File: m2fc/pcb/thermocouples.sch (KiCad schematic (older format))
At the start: 69 parts, among them IC301 AD8495, IC302 AD8656, IC303 AD8495, IC304 AD8656, IC305 AD8495, IC306 AD8656, P301 CONN_2, P302 CONN_2, P303 CONN_2

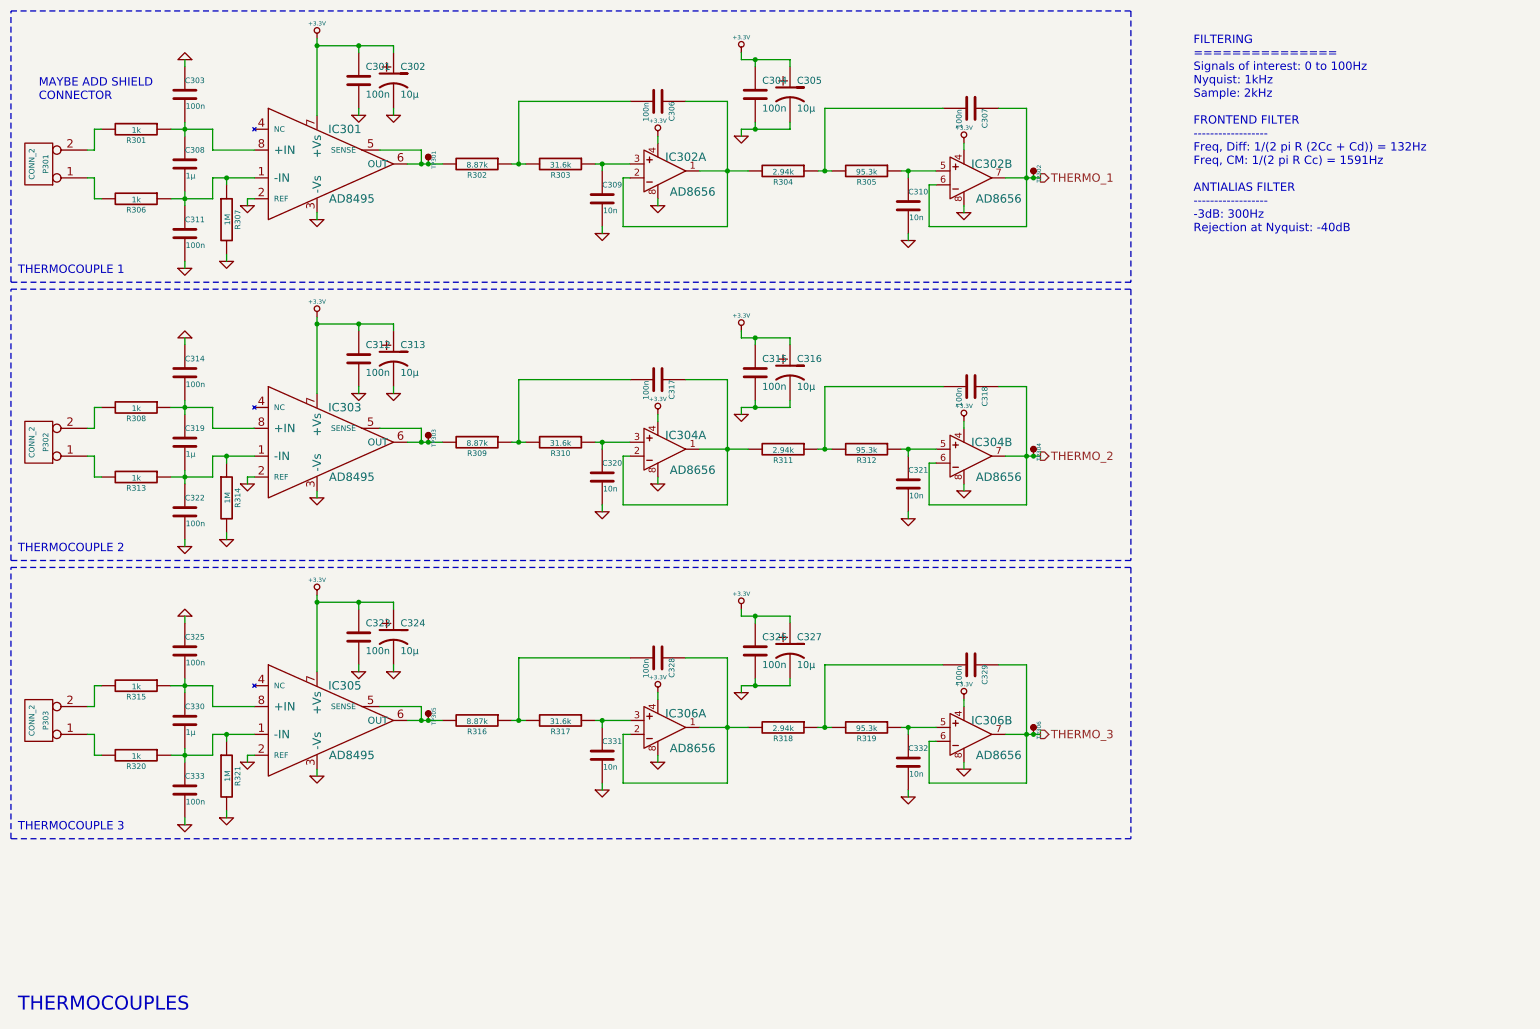
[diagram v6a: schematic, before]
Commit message: sd pullups, shielded sgs
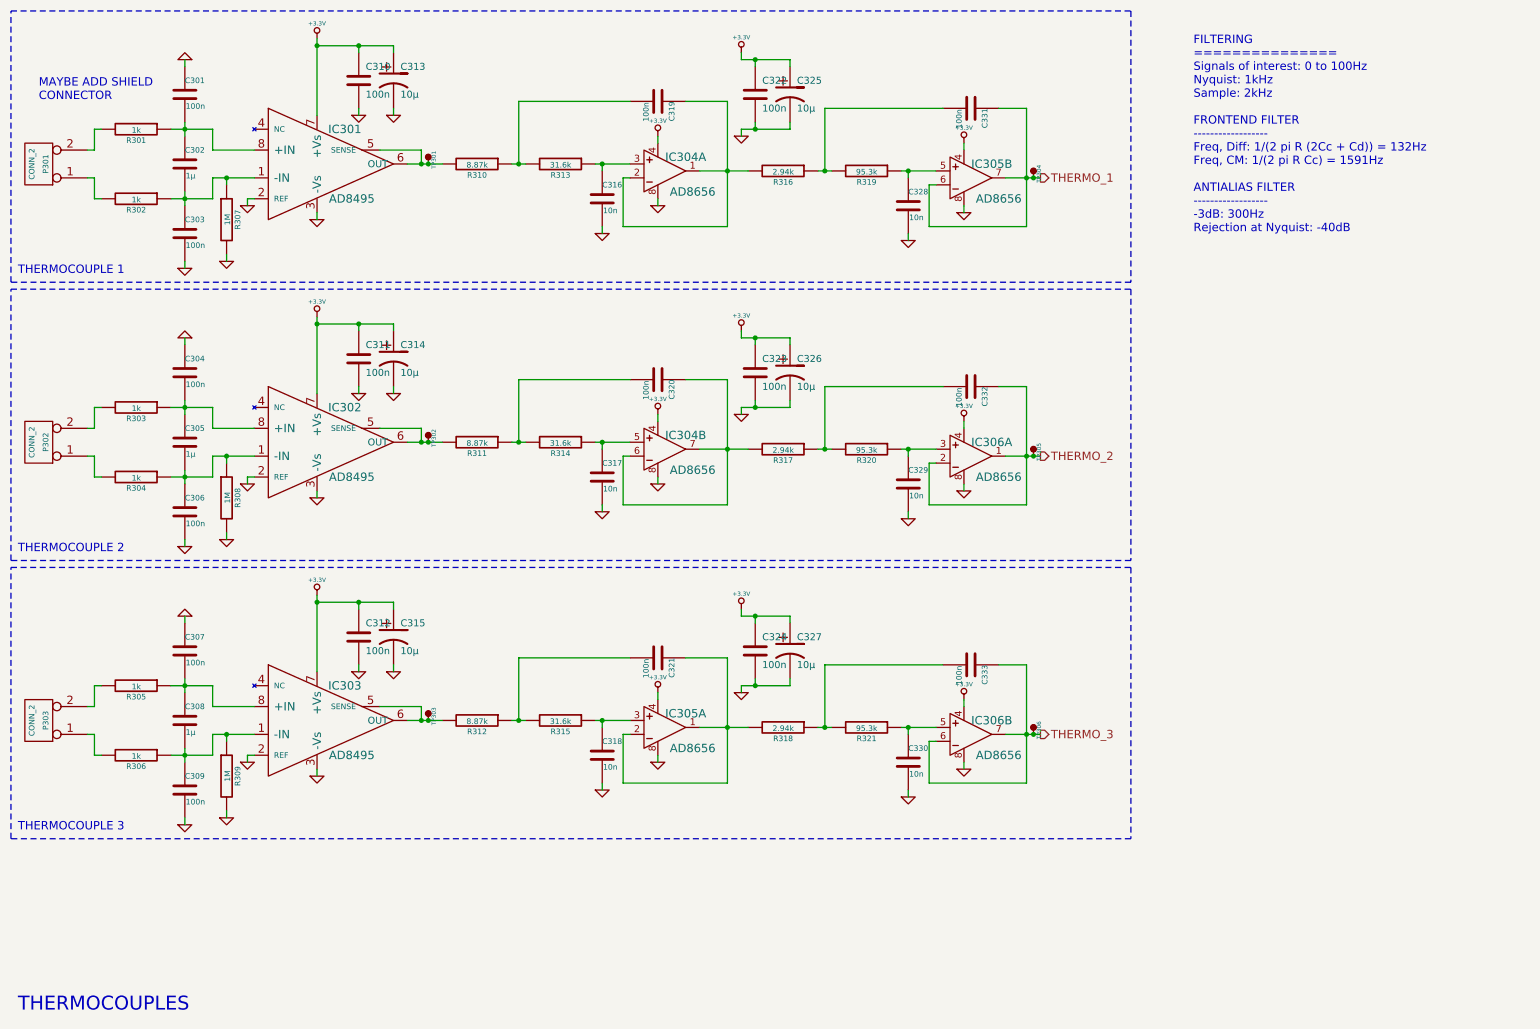
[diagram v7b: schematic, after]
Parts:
- C301: renamed from C303; footprint 1206 -> m2fc:C1206
- C302: renamed from C308; footprint 1206 -> m2fc:C1206
- C303: renamed from C311; footprint 1206 -> m2fc:C1206
- C304: renamed from C314; footprint 1206 -> m2fc:C1206
- C305: renamed from C319; footprint 1206 -> m2fc:C1206
- C306: renamed from C322; footprint 1206 -> m2fc:C1206
- C307: renamed from C325; footprint 1206 -> m2fc:C1206
- C308: renamed from C330; footprint 1206 -> m2fc:C1206
- C309: renamed from C333; footprint 1206 -> m2fc:C1206
- C310: renamed from C301; footprint 0603 -> m2fc:C0603
- C311: renamed from C312; footprint 0603 -> m2fc:C0603
- C312: renamed from C323; footprint 0603 -> m2fc:C0603
- C316: renamed from C309; footprint 0603 -> m2fc:C0603
- C317: renamed from C320; footprint 0603 -> m2fc:C0603
- C318: renamed from C331; footprint 0603 -> m2fc:C0603
- C319: renamed from C306; footprint 1206 -> m2fc:C1206
- C320: renamed from C317; footprint 1206 -> m2fc:C1206
- C321: renamed from C328; footprint 1206 -> m2fc:C1206
- C322: renamed from C304; footprint 0603 -> m2fc:C0603
- C323: renamed from C315; footprint 0603 -> m2fc:C0603
- C324: renamed from C326; footprint 0603 -> m2fc:C0603
- C328: renamed from C310; footprint 0603 -> m2fc:C0603
- C329: renamed from C321; footprint 0603 -> m2fc:C0603
- C330: renamed from C332; footprint 0603 -> m2fc:C0603
- C331: renamed from C307; footprint 1206 -> m2fc:C1206
- C332: renamed from C318; footprint 1206 -> m2fc:C1206
- C333: renamed from C329; footprint 1206 -> m2fc:C1206
- IC301: footprint 8MSOP -> m2fc:MSOP8
- IC302: renamed from IC303; footprint 8MSOP -> m2fc:MSOP8
- IC303: renamed from IC305; footprint 8MSOP -> m2fc:MSOP8
- IC304, IC305: renamed from IC302; footprint SOIC8 -> m2fc:SOIC8
- IC304, IC306: footprint SOIC8 -> m2fc:SOIC8
- IC305: renamed from IC306; footprint SOIC8 -> m2fc:SOIC8
- IC306: renamed from IC304; footprint SOIC8 -> m2fc:SOIC8
- P301, P302: footprint (none) -> m2fc:S02B-PASK-2
- P303: footprint (none) -> m2fc:S04B-PASK-2
- R301, R307, R318: footprint 0603 -> m2fc:R0603
- R302: renamed from R306; footprint 0603 -> m2fc:R0603
- R303: renamed from R308; footprint 0603 -> m2fc:R0603
- R304: renamed from R313; footprint 0603 -> m2fc:R0603
- R305: renamed from R315; footprint 0603 -> m2fc:R0603
- R306: renamed from R320; footprint 0603 -> m2fc:R0603
- R308: renamed from R314; footprint 0603 -> m2fc:R0603
- R309: renamed from R321; footprint 0603 -> m2fc:R0603
- R310: renamed from R302; footprint 0603 -> m2fc:R0603
- R311: renamed from R309; footprint 0603 -> m2fc:R0603
- R312: renamed from R316; footprint 0603 -> m2fc:R0603
- R313: renamed from R303; footprint 0603 -> m2fc:R0603
- R314: renamed from R310; footprint 0603 -> m2fc:R0603
- R315: renamed from R317; footprint 0603 -> m2fc:R0603
- R316: renamed from R304; footprint 0603 -> m2fc:R0603
- R317: renamed from R311; footprint 0603 -> m2fc:R0603
- R319: renamed from R305; footprint 0603 -> m2fc:R0603
- R320: renamed from R312; footprint 0603 -> m2fc:R0603
- R321: renamed from R319; footprint 0603 -> m2fc:R0603
- TP301, TP306: footprint (none) -> m2fc:TESTPAD
- TP302: renamed from TP303; footprint (none) -> m2fc:TESTPAD
- TP303: renamed from TP305; footprint (none) -> m2fc:TESTPAD
- TP304: renamed from TP302; footprint (none) -> m2fc:TESTPAD
- TP305: renamed from TP304; footprint (none) -> m2fc:TESTPAD
- renumbered C302 to C313, C313 to C314, C324 to C315, C305 to C325, C316 to C326
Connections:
- net THERMO_2: now also IC306.1 (OUT), IC306.2 (-IN); no longer IC306.6 (-IN), IC306.7 (OUT)
- net at C317.1, R314.1: now also IC304.5 (+IN); no longer IC304.3 (+IN)
- net at C320.1, R317.2: now also IC304.6 (-IN), IC304.7 (OUT); no longer IC304.1 (OUT), IC304.2 (-IN)
- net at C329.1, R320.1: now also IC306.3 (+IN); no longer IC306.5 (+IN)

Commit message: add esd diodes to m2fc
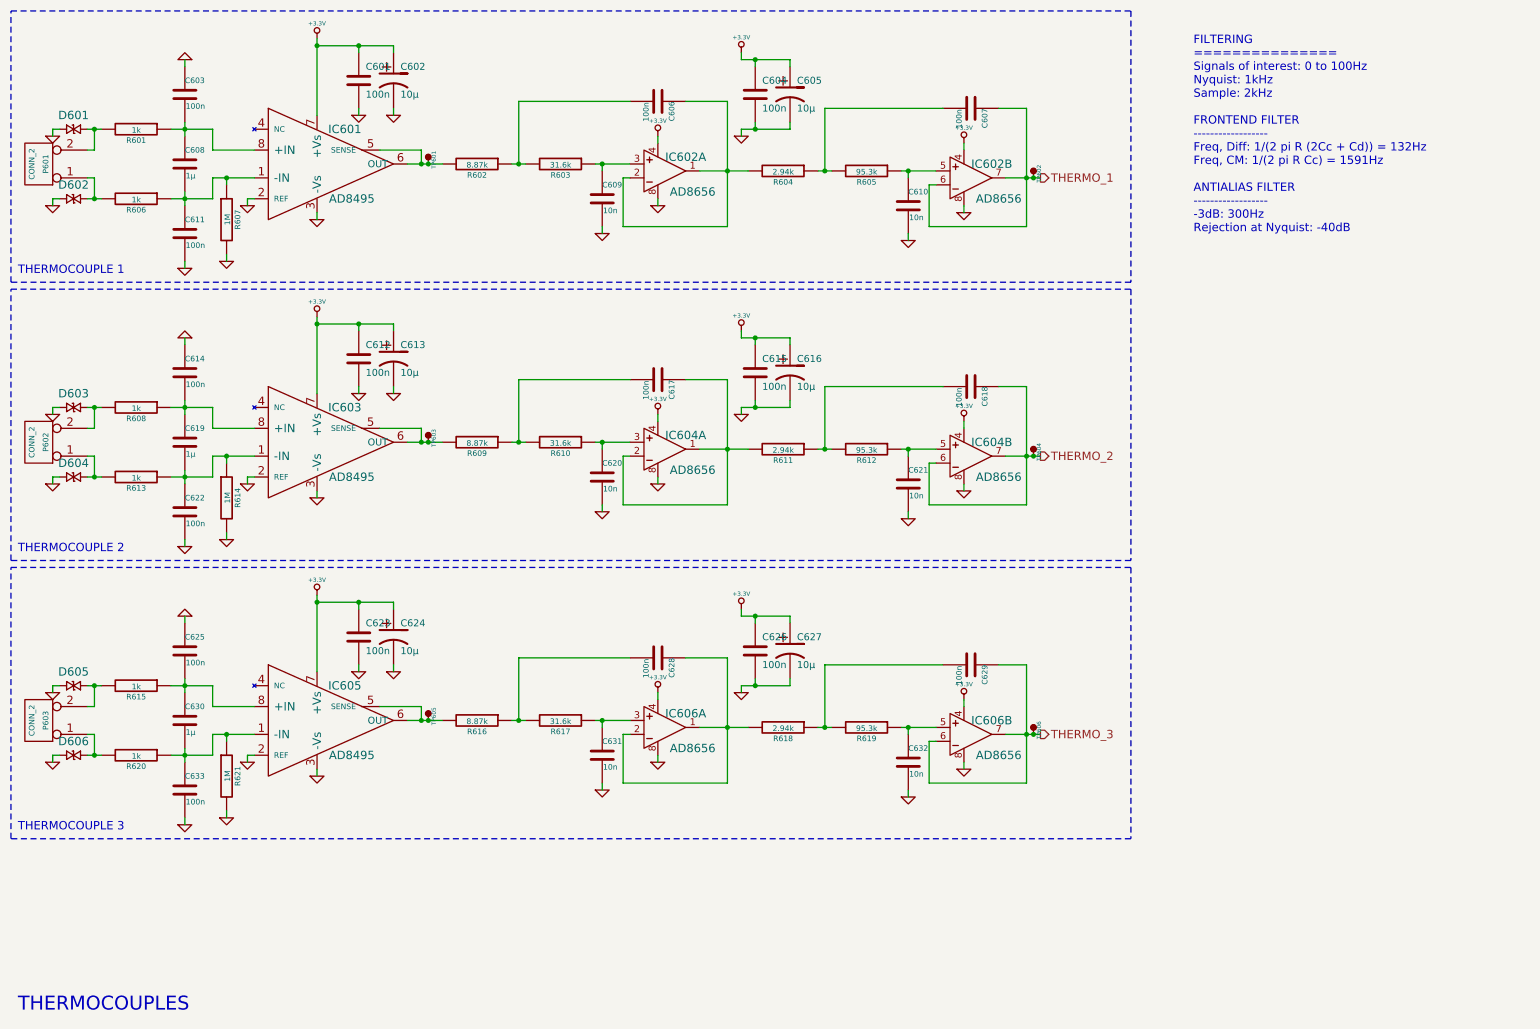
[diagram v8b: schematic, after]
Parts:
- added D601, D602, D603, D604, D605, D606: CGA0402MLC-12G, m2fc:R0402, symbol CGA0402MLC-12G
- C602: renamed from C313; footprint 1411 -> m2fc:C0603; Farnell 2333026 -> 1657936
- C605: renamed from C325; footprint 1411 -> m2fc:C0603; Farnell 2333026 -> 1657936
- C608: renamed from C302; footprint m2fc:C1206 -> m2fc:C0603; Farnell 2362126 -> 2346895
- C613: renamed from C314; footprint 1411 -> m2fc:C0603; Farnell 2333026 -> 1657936
- C616: renamed from C326; footprint 1411 -> m2fc:C0603; Farnell 2333026 -> 1657936
- C619: renamed from C305; footprint m2fc:C1206 -> m2fc:C0603; Farnell 2362126 -> 2346895
- C624: renamed from C315; footprint 1411 -> m2fc:C0603; Farnell 2333026 -> 1657936
- C627: renamed from C327; footprint 1411 -> m2fc:C0603; Farnell 2333026 -> 1657936
- C630: renamed from C308; footprint m2fc:C1206 -> m2fc:C0603; Farnell 2362126 -> 2346895
- P601: renamed from P301; Farnell 3810628 -> 1830747
- P602: renamed from P302; Farnell 3810628 -> 1830747
- P603: renamed from P303; footprint m2fc:S04B-PASK-2 -> m2fc:S02B-PASK-2; Farnell 3810628 -> 1830747
- renumbered C310 to C601, C301 to C603, C322 to C604, C319 to C606, C331 to C607, C316 to C609, C328 to C610, C303 to C611, C311 to C612, C304 to C614, C323 to C615, C320 to C617, C332 to C618, C317 to C620, C329 to C621, C306 to C622, C312 to C623, C307 to C625, C324 to C626, C321 to C628, C333 to C629, C318 to C631, C330 to C632, C309 to C633, IC301 to IC601, IC304 to IC602, IC305 to IC602, IC302 to IC603, IC304 to IC604, IC306 to IC604, IC303 to IC605, IC305 to IC606, IC306 to IC606, R301 to R601, R310 to R602, R313 to R603, R316 to R604, R319 to R605, R302 to R606, R307 to R607, R303 to R608, R311 to R609, R314 to R610, R317 to R611, R320 to R612, R304 to R613, R308 to R614, R305 to R615, R312 to R616, R315 to R617, R318 to R618, R321 to R619, R306 to R620, R309 to R621, TP301 to TP601, TP304 to TP602, TP302 to TP603, TP305 to TP604, TP303 to TP605, TP306 to TP606
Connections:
- net GND: now also D601.2, D602.2, D603.2, D604.2, D605.2, D606.2
- net THERMO_2: now also IC604.6 (-IN), IC604.7 (OUT); no longer IC604.1 (OUT), IC604.2 (-IN)
- net at P601.2 (PM), R601.2: now also D601.1
- net at P601.1 (P1), R606.2: now also D602.1
- net at P602.2 (PM), R608.2: now also D603.1
- net at P602.1 (P1), R613.2: now also D604.1
- net at C620.1, R610.1: now also IC604.3 (+IN); no longer IC604.5 (+IN)
- net at C617.1, R611.2: now also IC604.1 (OUT), IC604.2 (-IN); no longer IC604.6 (-IN), IC604.7 (OUT)
- net at C621.1, R612.1: now also IC604.5 (+IN); no longer IC604.3 (+IN)
- net at P603.2 (PM), R615.2: now also D605.1
- net at P603.1 (P1), R620.2: now also D606.1
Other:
- note removed: "MAYBE ADD SHIELD\nCONNECTOR"
